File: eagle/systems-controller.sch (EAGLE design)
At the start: 48 parts, among them IC1 MK20DX256VLH7, IC2 MKL02Z32VFG4, IC3 TPS6214XRGT, J1 SIG, J2 PWR, J3 GND, Q1 FA-238, Q2 PMV20ENR, Q3 PMV20ENR, Q4 PMV20ENR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

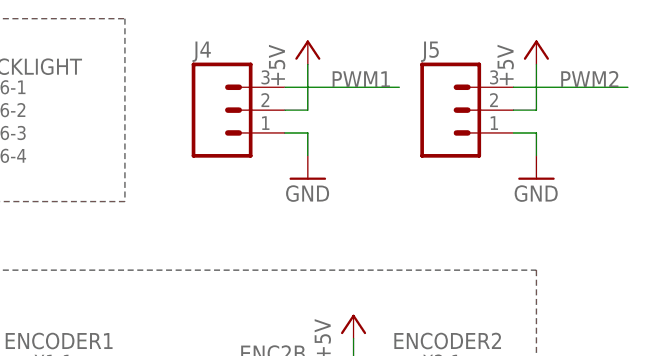
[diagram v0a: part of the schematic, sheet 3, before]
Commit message: added pwm headers
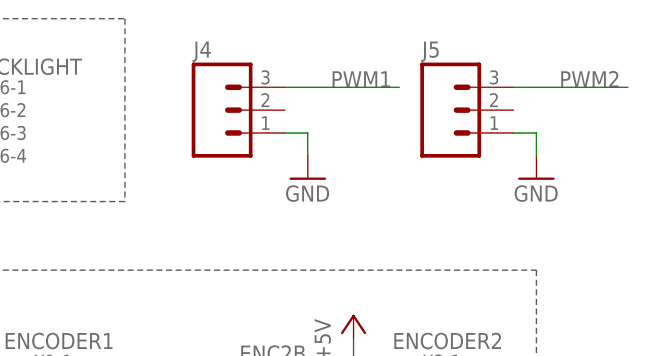
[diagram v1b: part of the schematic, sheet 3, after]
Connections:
- net +5V: no longer J4.2, J5.2
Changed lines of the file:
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@@
 <setting verticaltext="up"/>
 </settings>
-<grid distance="0.1" unitdist="inch" unit="inch" style="lines" multiple="1" display="yes" altdistance="0.01" altunitdist="inch" altunit="inch"/>
+<grid distance="0.1" unitdist="inch" unit="inch" style="lines" multiple="1" display="no" altdistance="0.01" altunitdist="inch" altunit="inch"/>
 <layers>
 <layer number="1" name="Top" color="4" fill="10" visible="no" active="no"/>
@@
 <part name="GND22" library="supply1" deviceset="GND" device=""/>
 <part name="GND23" library="supply1" deviceset="GND" device=""/>
-<part name="P+6" library="supply1" deviceset="+5V" device=""/>
-<part name="P+7" library="supply1" deviceset="+5V" device=""/>
 </parts>
 <sheets>
@@
 <instance part="GND22" gate="1" x="165.1" y="68.58"/>
 <instance part="GND23" gate="1" x="190.5" y="68.58"/>
-<instance part="P+6" gate="1" x="165.1" y="83.82"/>
-<instance part="P+7" gate="1" x="190.5" y="83.82"/>
 </instances>
 <busses>
@@
 <wire x1="170.18" y1="45.72" x2="170.18" y2="50.8" width="0.1524" layer="91"/>
 </segment>
-<segment>
-<pinref part="J4" gate="J$1" pin="2"/>
-<pinref part="P+6" gate="1" pin="+5V"/>
-<wire x1="162.56" y1="76.2" x2="165.1" y2="76.2" width="0.1524" layer="91"/>
-<wire x1="165.1" y1="76.2" x2="165.1" y2="81.28" width="0.1524" layer="91"/>
-</segment>
-<segment>
-<pinref part="P+7" gate="1" pin="+5V"/>
-<pinref part="J5" gate="J$1" pin="2"/>
-<wire x1="187.96" y1="76.2" x2="190.5" y2="76.2" width="0.1524" layer="91"/>
-<wire x1="190.5" y1="76.2" x2="190.5" y2="81.28" width="0.1524" layer="91"/>
-</segment>
-</net>
+</net>

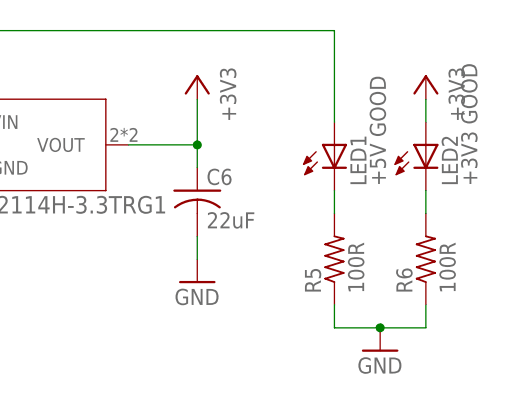
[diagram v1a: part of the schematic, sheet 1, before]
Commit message: made silkscreen pretty!
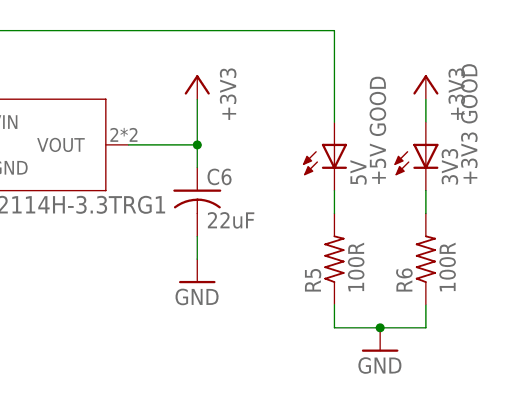
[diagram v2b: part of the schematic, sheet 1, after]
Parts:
- renumbered LED1 to 5V, LED2 to 3V3
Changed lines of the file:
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@@
 <part name="P+2" library="supply1" deviceset="+5V" device=""/>
 <part name="P+3" library="supply1" deviceset="+5V" device=""/>
-<part name="LED1" library="led" deviceset="LED" device="SML0603" value="+5V GOOD"/>
-<part name="LED2" library="led" deviceset="LED" device="SML0603" value="+3V3 GOOD"/>
+<part name="5V" library="led" deviceset="LED" device="SML0603" value="+5V GOOD"/>
+<part name="3V3" library="led" deviceset="LED" device="SML0603" value="+3V3 GOOD"/>
 <part name="R5" library="resistor" deviceset="R-US_" device="R0603" value="100R"/>
 <part name="R6" library="resistor" deviceset="R-US_" device="R0603" value="100R"/>
@@
 <instance part="+3V1" gate="G$1" x="180.34" y="60.96" rot="MR0"/>
 <instance part="P+2" gate="1" x="137.16" y="63.5"/>
-<instance part="LED1" gate="G$1" x="195.58" y="53.34"/>
-<instance part="LED2" gate="G$1" x="205.74" y="53.34"/>
+<instance part="5V" gate="G$1" x="195.58" y="53.34"/>
+<instance part="3V3" gate="G$1" x="205.74" y="53.34"/>
 <instance part="R5" gate="G$1" x="195.58" y="40.64" rot="R90"/>
 <instance part="R6" gate="G$1" x="205.74" y="40.64" rot="R90"/>
@@
 </segment>
 <segment>
-<pinref part="LED2" gate="G$1" pin="A"/>
+<pinref part="3V3" gate="G$1" pin="A"/>
 <pinref part="+3V4" gate="G$1" pin="+3V3"/>
 <wire x1="205.74" y1="55.88" x2="205.74" y2="58.42" width="0.1524" layer="91"/>
@@
 <wire x1="132.08" y1="55.88" x2="149.86" y2="55.88" width="0.1524" layer="91"/>
 <label x="139.7" y="55.88" size="1.778" layer="95"/>
-<pinref part="LED1" gate="G$1" pin="A"/>
+<pinref part="5V" gate="G$1" pin="A"/>
 <wire x1="149.86" y1="55.88" x2="152.4" y2="55.88" width="0.1524" layer="91"/>
 <wire x1="195.58" y1="55.88" x2="195.58" y2="66.04" width="0.1524" layer="91"/>
@@
 <net name="N$23" class="0">
 <segment>
-<pinref part="LED1" gate="G$1" pin="C"/>
+<pinref part="5V" gate="G$1" pin="C"/>
 <pinref part="R5" gate="G$1" pin="2"/>
 <wire x1="195.58" y1="48.26" x2="195.58" y2="45.72" width="0.1524" layer="91"/>
@@
 <net name="N$24" class="0">
 <segment>
-<pinref part="LED2" gate="G$1" pin="C"/>
+<pinref part="3V3" gate="G$1" pin="C"/>
 <pinref part="R6" gate="G$1" pin="2"/>
 <wire x1="205.74" y1="48.26" x2="205.74" y2="45.72" width="0.1524" layer="91"/>

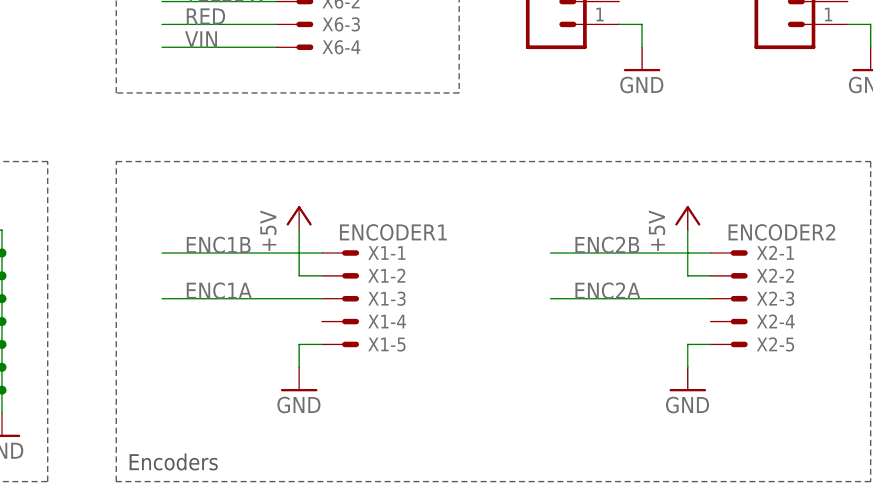
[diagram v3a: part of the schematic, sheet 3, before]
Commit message: fixed reversed encoder connectors
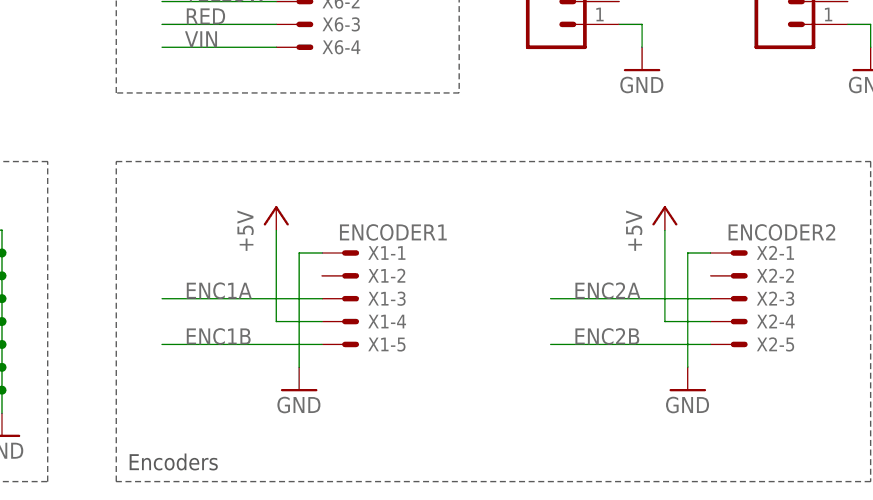
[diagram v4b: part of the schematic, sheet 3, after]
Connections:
- net +5V: now also X1-4.S, X2-4.S; no longer X1-2.S, X2-2.S
- net ENC1B: now also X1-5.S; no longer X1-1.S
- net ENC2B: now also X2-5.S; no longer X2-1.S
- net GND: now also X1-1.S, X2-1.S; no longer X1-5.S, X2-5.S
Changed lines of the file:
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@@
 <part name="GND14" library="supply1" deviceset="GND" device=""/>
 <part name="+3V4" library="supply1" deviceset="+3V3" device=""/>
-<part name="GND15" library="supply1" deviceset="GND" device=""/>
 <part name="GND16" library="supply1" deviceset="GND" device=""/>
-<part name="P+4" library="supply1" deviceset="+5V" device=""/>
 <part name="P+5" library="supply1" deviceset="+5V" device=""/>
 <part name="Q2" library="SparkFun-DiscreteSemi" deviceset="MOSFET-NCHANNEL" device="AO3404A" value="PMV20ENR"/>
@@
 <part name="GND22" library="supply1" deviceset="GND" device=""/>
 <part name="GND23" library="supply1" deviceset="GND" device=""/>
+<part name="GND15" library="supply1" deviceset="GND" device=""/>
+<part name="P+4" library="supply1" deviceset="+5V" device=""/>
 </parts>
 <sheets>
@@
 <instance part="GND11" gate="1" x="93.98" y="27.94"/>
 <instance part="P+3" gate="1" x="73.66" y="55.88"/>
-<instance part="GND15" gate="1" x="127" y="33.02"/>
 <instance part="GND16" gate="1" x="170.18" y="33.02"/>
-<instance part="P+4" gate="1" x="127" y="53.34"/>
-<instance part="P+5" gate="1" x="170.18" y="53.34"/>
+<instance part="P+5" gate="1" x="167.64" y="53.34"/>
 <instance part="X6" gate="-1" x="127" y="78.74"/>
 <instance part="X6" gate="-2" x="127" y="76.2"/>
@@
 <instance part="GND22" gate="1" x="165.1" y="68.58"/>
 <instance part="GND23" gate="1" x="190.5" y="68.58"/>
+<instance part="GND15" gate="1" x="127" y="33.02"/>
+<instance part="P+4" gate="1" x="124.46" y="53.34"/>
 </instances>
 <busses>
@@
 </segment>
 <segment>
-<pinref part="X2" gate="-5" pin="S"/>
 <pinref part="GND16" gate="1" pin="GND"/>
-<wire x1="172.72" y1="38.1" x2="170.18" y2="38.1" width="0.1524" layer="91"/>
-<wire x1="170.18" y1="38.1" x2="170.18" y2="35.56" width="0.1524" layer="91"/>
-</segment>
-<segment>
-<pinref part="X1" gate="-5" pin="S"/>
-<pinref part="GND15" gate="1" pin="GND"/>
-<wire x1="129.54" y1="38.1" x2="127" y2="38.1" width="0.1524" layer="91"/>
-<wire x1="127" y1="38.1" x2="127" y2="35.56" width="0.1524" layer="91"/>
+<pinref part="X2" gate="-1" pin="S"/>
+<wire x1="172.72" y1="48.26" x2="170.18" y2="48.26" width="0.1524" layer="91"/>
+<wire x1="170.18" y1="48.26" x2="170.18" y2="35.56" width="0.1524" layer="91"/>
 </segment>
 <segment>
@@
 <wire x1="187.96" y1="73.66" x2="190.5" y2="73.66" width="0.1524" layer="91"/>
 <wire x1="190.5" y1="73.66" x2="190.5" y2="71.12" width="0.1524" layer="91"/>
+</segment>
+<segment>
+<pinref part="X1" gate="-1" pin="S"/>
+<pinref part="GND15" gate="1" pin="GND"/>
+<wire x1="129.54" y1="48.26" x2="127" y2="48.26" width="0.1524" layer="91"/>
+<wire x1="127" y1="48.26" x2="127" y2="35.56" width="0.1524" layer="91"/>
 </segment>
 </net>
@@
 </segment>
 <segment>
-<pinref part="X1" gate="-2" pin="S"/>
+<pinref part="X1" gate="-4" pin="S"/>
 <pinref part="P+4" gate="1" pin="+5V"/>
-<wire x1="129.54" y1="45.72" x2="127" y2="45.72" width="0.1524" layer="91"/>
-<wire x1="127" y1="45.72" x2="127" y2="50.8" width="0.1524" layer="91"/>
-</segment>
-<segment>
-<pinref part="X2" gate="-2" pin="S"/>
+<wire x1="129.54" y1="40.64" x2="124.46" y2="40.64" width="0.1524" layer="91"/>
+<wire x1="124.46" y1="40.64" x2="124.46" y2="50.8" width="0.1524" layer="91"/>
+</segment>
+<segment>
+<pinref part="X2" gate="-4" pin="S"/>
 <pinref part="P+5" gate="1" pin="+5V"/>
-<wire x1="172.72" y1="45.72" x2="170.18" y2="45.72" width="0.1524" layer="91"/>
-<wire x1="170.18" y1="45.72" x2="170.18" y2="50.8" width="0.1524" layer="91"/>
+<wire x1="172.72" y1="40.64" x2="167.64" y2="40.64" width="0.1524" layer="91"/>
+<wire x1="167.64" y1="40.64" x2="167.64" y2="50.8" width="0.1524" layer="91"/>
 </segment>
 </net>
@@
 </segment>
 </net>
-<net name="ENC1B" class="0">
-<segment>
-<pinref part="X1" gate="-1" pin="S"/>
-<wire x1="129.54" y1="48.26" x2="111.76" y2="48.26" width="0.1524" layer="91"/>
-<label x="114.3" y="48.26" size="1.778" layer="95"/>
+<net name="GREEN" class="0">
+<segment>
+<pinref part="X6" gate="-1" pin="S"/>
+<wire x1="124.46" y1="78.74" x2="111.76" y2="78.74" width="0.1524" layer="91"/>
+<label x="114.3" y="78.74" size="1.778" layer="95"/>
+</segment>
+</net>
+<net name="YELLOW" class="0">
+<segment>
+<pinref part="X6" gate="-2" pin="S"/>
+<wire x1="111.76" y1="76.2" x2="124.46" y2="76.2" width="0.1524" layer="91"/>
+<label x="114.3" y="76.2" size="1.778" layer="95"/>
+</segment>
+</net>
+<net name="RED" class="0">
+<segment>
+<pinref part="X6" gate="-3" pin="S"/>
+<wire x1="124.46" y1="73.66" x2="111.76" y2="73.66" width="0.1524" layer="91"/>
+<label x="114.3" y="73.66" size="1.778" layer="95"/>
+</segment>
+</net>
+<net name="VIN" class="0">
+<segment>
+<pinref part="X6" gate="-4" pin="S"/>
+<wire x1="111.76" y1="71.12" x2="124.46" y2="71.12" width="0.1524" layer="91"/>
+<label x="114.3" y="71.12" size="1.778" layer="95"/>
+</segment>
+</net>
+<net name="PWM2" class="0">
+<segment>
+<pinref part="J5" gate="J$1" pin="3"/>
+<wire x1="187.96" y1="78.74" x2="200.66" y2="78.74" width="0.1524" layer="91"/>
+<label x="193.04" y="78.74" size="1.778" layer="95"/>
+</segment>
+</net>
+<net name="PWM1" class="0">
+<segment>
+<pinref part="J4" gate="J$1" pin="3"/>
+<wire x1="162.56" y1="78.74" x2="175.26" y2="78.74" width="0.1524" layer="91"/>
+<label x="167.64" y="78.74" size="1.778" layer="95"/>
 </segment>
 </net>
@@
 </segment>
 </net>
+<net name="ENC1B" class="0">
+<segment>
+<pinref part="X1" gate="-5" pin="S"/>
+<wire x1="111.76" y1="38.1" x2="129.54" y2="38.1" width="0.1524" layer="91"/>
+<label x="114.3" y="38.1" size="1.778" layer="95"/>
+</segment>
+</net>
 <net name="ENC2B" class="0">
 <segment>
-<pinref part="X2" gate="-1" pin="S"/>
-<wire x1="172.72" y1="48.26" x2="154.94" y2="48.26" width="0.1524" layer="91"/>
-<label x="157.48" y="48.26" size="1.778" layer="95"/>
+<pinref part="X2" gate="-5" pin="S"/>
+<wire x1="172.72" y1="38.1" x2="154.94" y2="38.1" width="0.1524" layer="91"/>
+<label x="157.48" y="38.1" size="1.778" layer="95"/>
 </segment>
 </net>
@@
 <segment>
 <pinref part="X2" gate="-3" pin="S"/>
-<wire x1="172.72" y1="43.18" x2="154.94" y2="43.18" width="0.1524" layer="91"/>
+<wire x1="154.94" y1="43.18" x2="172.72" y2="43.18" width="0.1524" layer="91"/>
 <label x="157.48" y="43.18" size="1.778" layer="95"/>
 </segment>
 </net>
-<net name="GREEN" class="0">
-<segment>
-<pinref part="X6" gate="-1" pin="S"/>
-<wire x1="124.46" y1="78.74" x2="111.76" y2="78.74" width="0.1524" layer="91"/>
-<label x="114.3" y="78.74" size="1.778" layer="95"/>
-</segment>
-</net>
-<net name="YELLOW" class="0">
-<segment>
-<pinref part="X6" gate="-2" pin="S"/>
-<wire x1="111.76" y1="76.2" x2="124.46" y2="76.2" width="0.1524" layer="91"/>
-<label x="114.3" y="76.2" size="1.778" layer="95"/>
-</segment>
-</net>
-<net name="RED" class="0">
-<segment>
-<pinref part="X6" gate="-3" pin="S"/>
-<wire x1="124.46" y1="73.66" x2="111.76" y2="73.66" width="0.1524" layer="91"/>
-<label x="114.3" y="73.66" size="1.778" layer="95"/>
-</segment>
-</net>
-<net name="VIN" class="0">
-<segment>
-<pinref part="X6" gate="-4" pin="S"/>
-<wire x1="111.76" y1="71.12" x2="124.46" y2="71.12" width="0.1524" layer="91"/>
-<label x="114.3" y="71.12" size="1.778" layer="95"/>
-</segment>
-</net>
-<net name="PWM2" class="0">
-<segment>
-<pinref part="J5" gate="J$1" pin="3"/>
-<wire x1="187.96" y1="78.74" x2="200.66" y2="78.74" width="0.1524" layer="91"/>
-<label x="193.04" y="78.74" size="1.778" layer="95"/>
-</segment>
-</net>
-<net name="PWM1" class="0">
-<segment>
-<pinref part="J4" gate="J$1" pin="3"/>
-<wire x1="162.56" y1="78.74" x2="175.26" y2="78.74" width="0.1524" layer="91"/>
-<label x="167.64" y="78.74" size="1.778" layer="95"/>
-</segment>
-</net>
